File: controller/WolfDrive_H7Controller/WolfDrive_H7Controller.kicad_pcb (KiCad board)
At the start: 4 copper layers, 167.6 x 111.8 mm, 319 parts, among them CN10 CONN_02X17, CN7 CONN_02X10, CN8 CONN_02X08, CN9 CONN_02X15, CON1 SD_Card, J1 USB_OTG, J10 GND, J11 GND, J12 5V, J13 Regen, J14 Throttle, J15 PWM1, J16 PWM2, J17 PWM3, J18 ~PWM1, J19 ~PWM2, J2 QSPI_CLK, J20 ~PWM3, J21 OCV, J22 ~F_C, J23 ~F_B, J24 ~F_A, J25 Overtemp, J26 PWM_EN, J27 Conn_01x04_Female, J28 GS3, J29 Conn_01x04, J3 QSPI_NCS, J30 SPI2_SCK, J31 SPI2_NSS, J32 SPI2_MOSI, J33 SPI2_MISO, J34 PS-DIS, J35 3V3, J36 GND, J37 GND, J38 AGND, J39 SP1_MISO, J4 QSPI_IO0, J40 SP1_SCK, J41 SP1_NSS, J42 SP1_MOSI, J43 GS3, J44 GS3, J45 GS3, J46 GS3, J47 GS3, J48 GS3, J49 GS3, J5 QSPI_IO1, J50 GS3, J51 GS3, J52 GS3, J53 GS3, J54 GS3, J55 GS3, J6 QSPI_IO2, J7 QSPI_IO3, J8 12V, J9 GND, P1 GATE_IO_A, P10 GATE_IO_A, P11 GATE_IO_A, P7 CONN_01X02, P9 GATE_IO_A, U1 LM1117-5.0, U10 74HC266, U11 FT232RL, U12 74LVC1G02, U13 74LVC1G02, U14 74LVC1G02, U15 74LVC1G02, U16 74LVC1G02, U17 74LVC1G02, U18 74LVC1G02, U19 74LVC1G02, U2 LM1117-3.3, U21 74LVC1G02, U3 MCP101-315D, U4 LTV-356T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

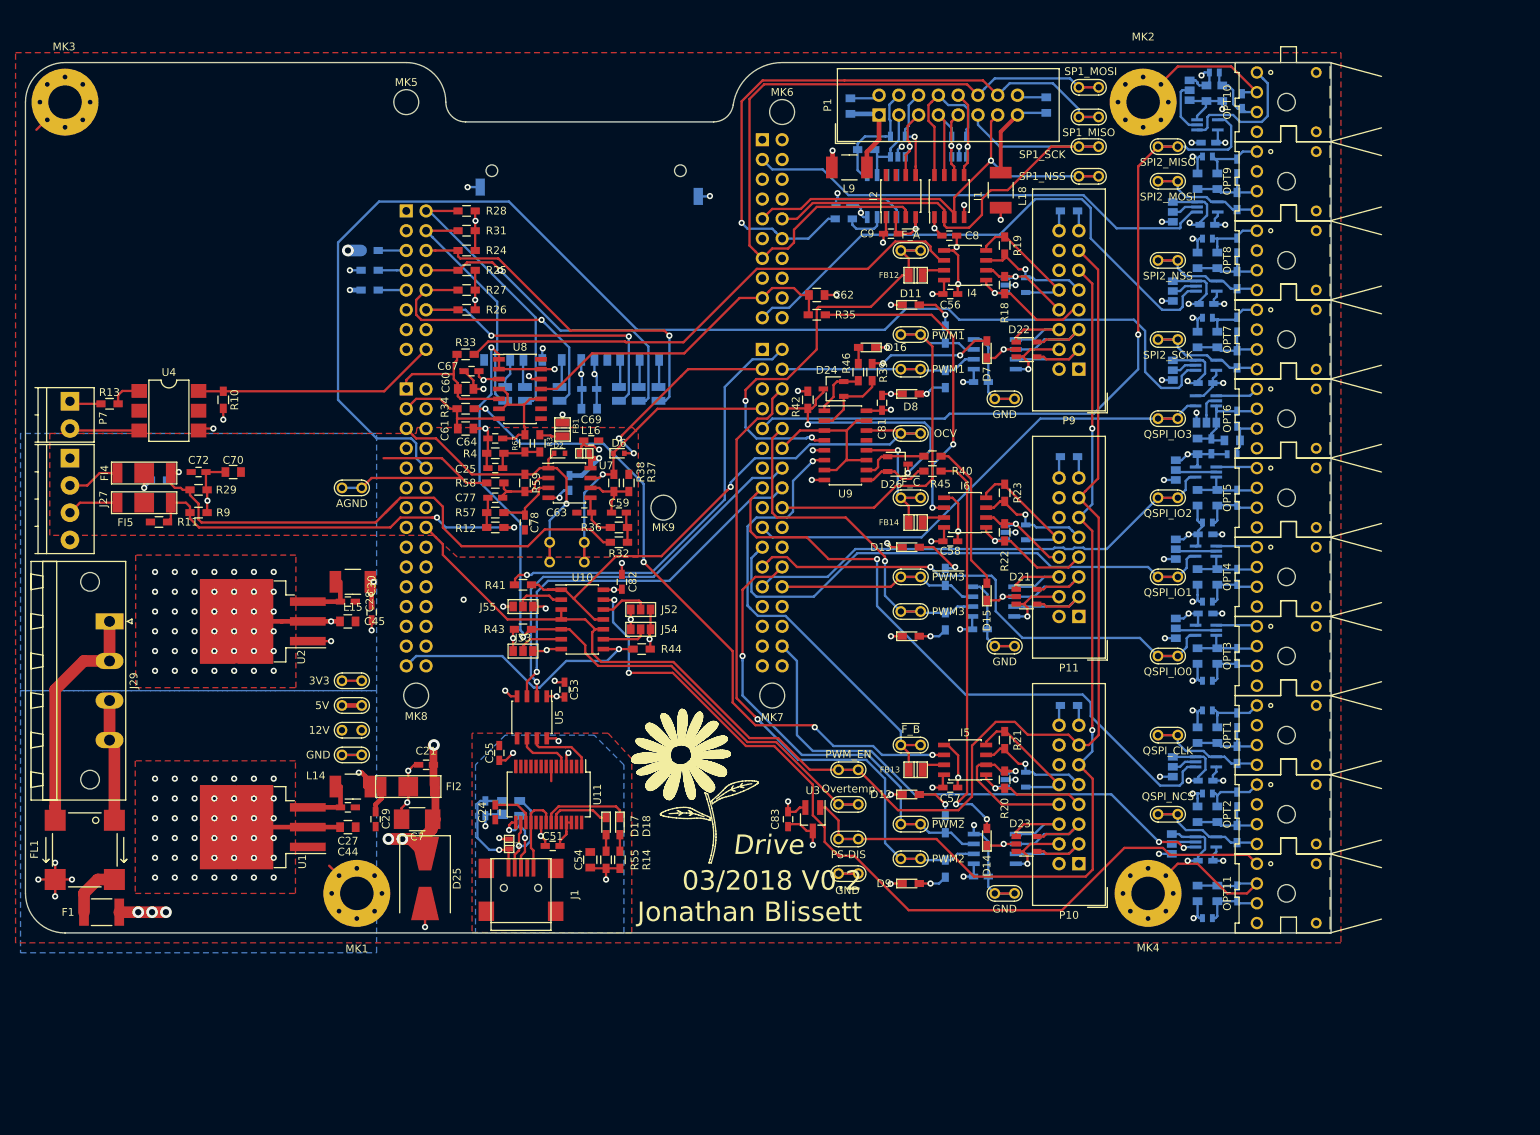
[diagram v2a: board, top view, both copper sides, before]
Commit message: Finished layout, silk sceen amended
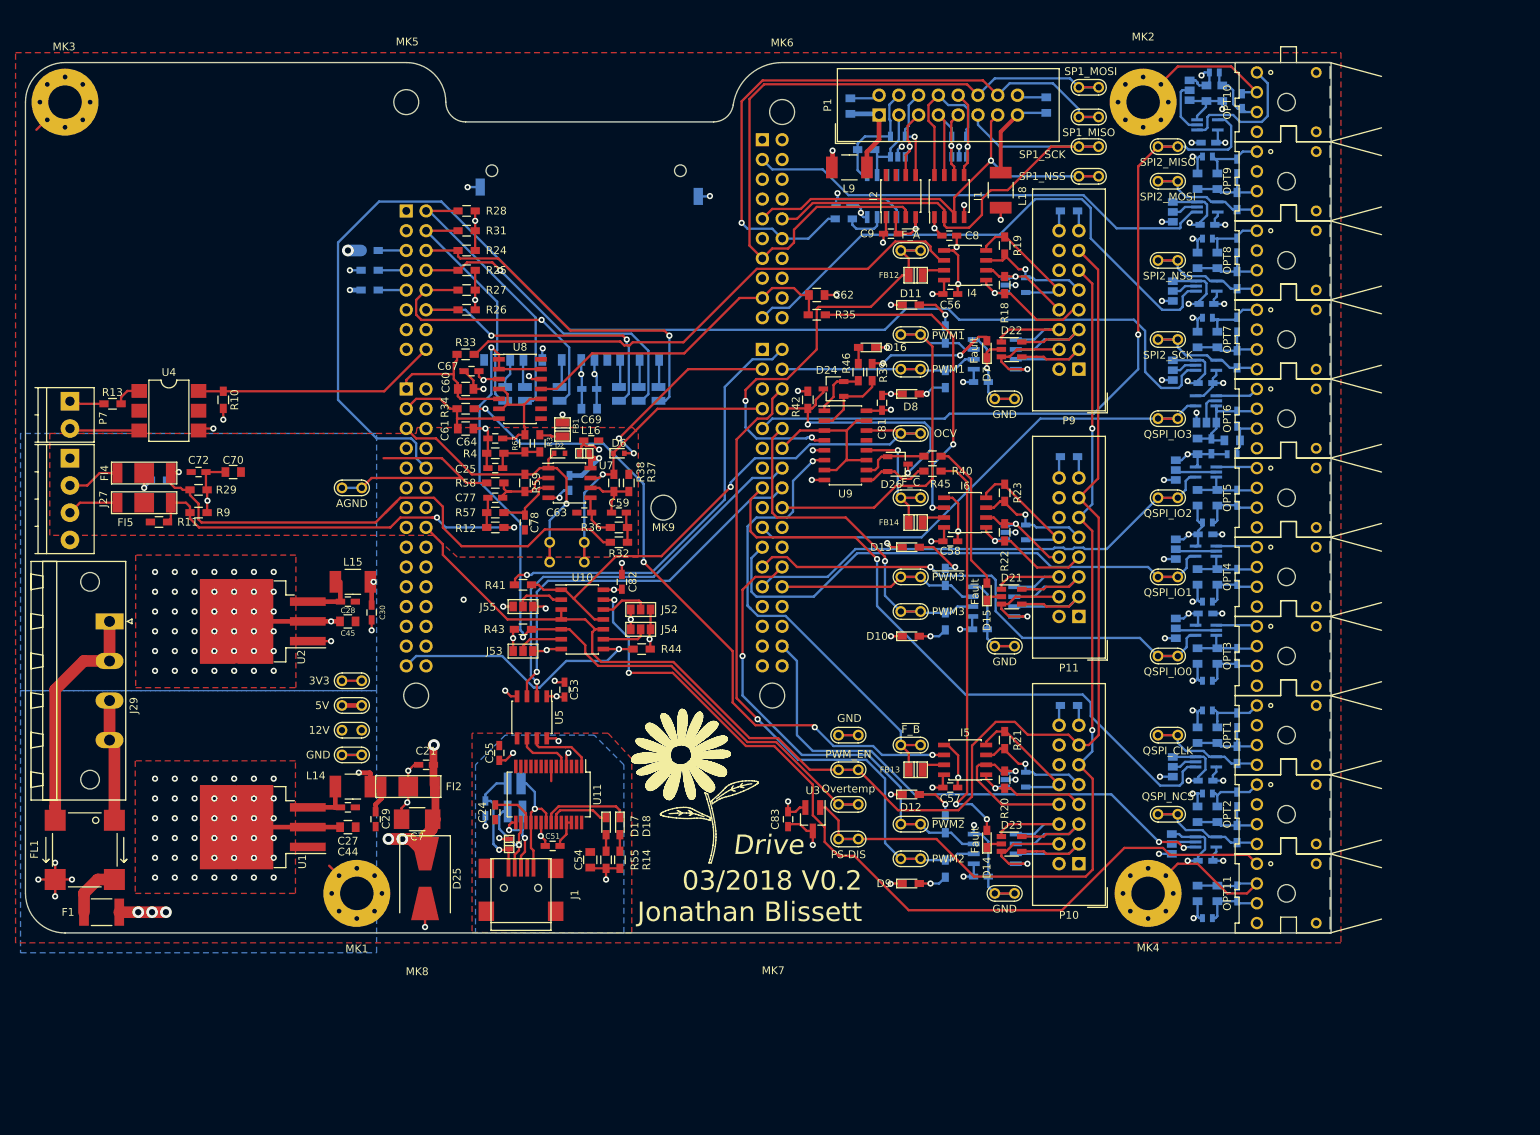
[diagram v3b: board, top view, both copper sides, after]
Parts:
- D1: footprint TO_SOT_Packages_SMD:SOT-143 -> Package_TO_SOT_SMD:SOT-143R_Reverse_Handsoldering
- moved J36 18.0 mm to (54.2, 5.08), turned to 0 degrees
- moved D21 1.91 mm to (76.5, -12.7)
- moved D22 1.91 mm to (76.5, -44.5)
- moved D23 1.91 mm to (76.5, 19.1)
- moved D1 1.49 mm to (12.7, 13.1), turned to 270 degrees
- moved R13 0.38 mm to (-39.0, -37.5)
- moved D14 0.25 mm to (73.3, 18.4)
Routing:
- net +5V: track 203.4 -> 188.8 mm
- net DGND: track 437.6 -> 432.9 mm, vias 63 -> 61
- net /PWMC_HS-: track 9.36 -> 13.9 mm
- net /PWMB_HS-: track 9.21 -> 13.7 mm
- net /PWMA_HS-: track 10.3 -> 14.5 mm
- net Net-(D7-Pad2): track 15.9 -> 18.8 mm
- net Net-(C10-Pad2): track 20.0 -> 22.6 mm, vias 1 -> 2
- net +12V: track 385.7 -> 383.3 mm
- net /PWMC_LS-: track 12.8 -> 14.7 mm
- net /PWMC_LS+: track 15.4 -> 17.3 mm
- net /PWMC_HS+: track 14.9 -> 16.8 mm
- net /PWMB_LS-: track 12.6 -> 14.5 mm
- net /PWMB_LS+: track 15.2 -> 17.1 mm
- net /PWMB_HS+: track 14.7 -> 16.6 mm
- net /PWMA_LS-: track 12.6 -> 14.5 mm
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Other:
- board text added: "D10"
- board text added: "Fault"

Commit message: Minor edits before fabricating v0.2
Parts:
- moved L14 0.25 mm to (-8.38, 11.7)
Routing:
- net /SPI2_SCK_PD3: track 165.4 -> 163.9 mm
- net Net-(I5-Pad6): track 88.5 -> 89.4 mm
- net /SP1_MISO_PA6: track 87.9 -> 87.0 mm
- net +5V: track 188.8 -> 189.5 mm
- net /TMR1_CH2N_PE10: track 67.8 -> 67.3 mm
- net /QUADSPI_BK1_NCS_PB10: track 69.4 -> 69.9 mm
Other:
- board text removed: "02/2018 V0.1 Jonathan Blissett"
